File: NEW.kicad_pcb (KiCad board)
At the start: 2 copper layers, 106 x 80 mm, 16 parts, among them J1 Screw_Terminal_01x16, J2 Screw_Terminal_01x16, J3 buck converter, J4 Infrared, J5 BMI, J6 light sensor, Q1 PN2222A, U1 LM1117T-5.0, U2 ESP32-CAM

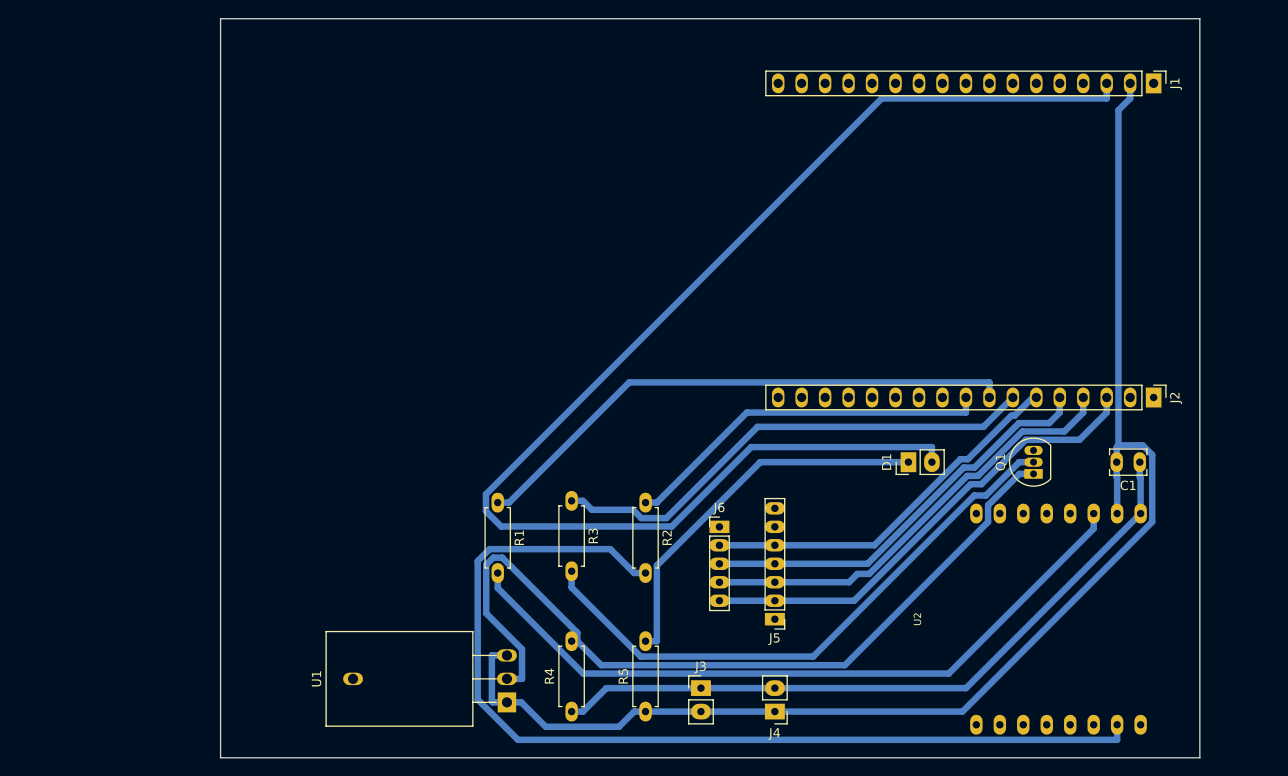
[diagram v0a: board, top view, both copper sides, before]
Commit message: added mounting holes
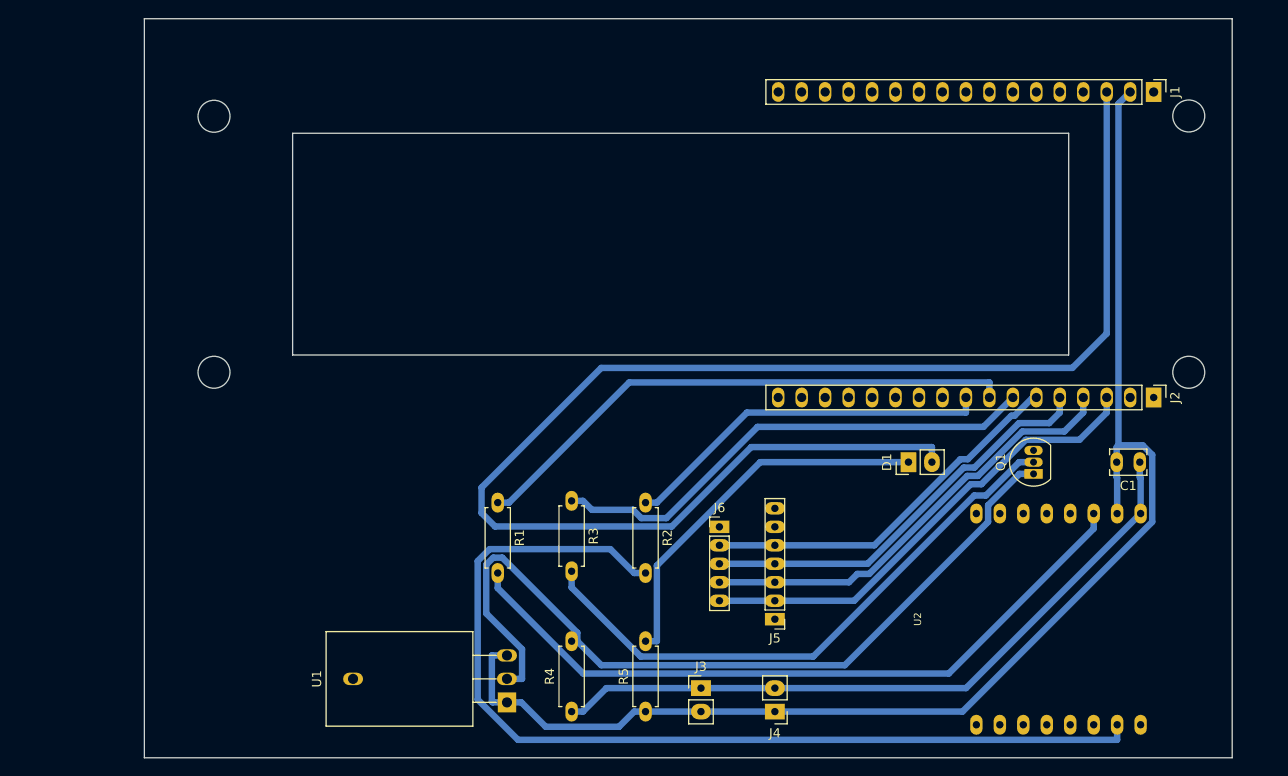
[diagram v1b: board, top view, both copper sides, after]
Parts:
- moved J1 0.93 mm to (219.0, 53.9)
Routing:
- net Net-(D1-A): track 142.6 -> 158.0 mm
- net GND: track 147.0 -> 146.0 mm
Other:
- board size 106 x 80 mm -> 117.8 x 80 mm
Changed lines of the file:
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@@
 	(footprint "Connector_PinHeader_2.54mm:PinHeader_1x17_P2.54mm_Vertical"
 		(layer "F.Cu")
-		(at 219 53 -90)
+		(at 219 53.93 -90)
 		(descr "Through hole straight pin header, 1x17, 2.54mm pitch, single row")
 		(tags "Through hole pin header THT 1x17 2.54mm single row")
@@
 	)
 	(gr_rect
-		(start 118 46)
-		(end 224 126)
+		(start 109.75 46)
+		(end 227.5 126)
+		(stroke
+			(width 0.05)
+			(type default)
+		)
+		(fill none)
+		(layer "Edge.Cuts")
+	)
+	(gr_circle
+		(center 222.8 56.53)
+		(end 221.07 56.53)
+		(stroke
+			(width 0.05)
+			(type default)
+		)
+		(fill none)
+		(layer "Edge.Cuts")
+	)
+	(gr_circle
+		(center 117.29 56.56)
+		(end 115.56 56.56)
+		(stroke
+			(width 0.05)
+			(type default)
+		)
+		(fill none)
+		(layer "Edge.Cuts")
+	)
+	(gr_circle
+		(center 117.29 84.27)
+		(end 115.56 84.27)
+		(stroke
+			(width 0.05)
+			(type default)
+		)
+		(fill none)
+		(layer "Edge.Cuts")
+	)
+	(gr_rect
+		(start 125.8 58.4)
+		(end 209.8 82.4)
+		(stroke
+			(width 0.05)
+			(type default)
+		)
+		(fill none)
+		(layer "Edge.Cuts")
+	)
+	(gr_circle
+		(center 222.8 84.27)
+		(end 221.07 84.27)
 		(stroke
 			(width 0.05)
@@
 	)
 	(segment
-		(start 215.19 55.9017)
-		(end 215.19 92.1783)
-		(width 0.7)
-		(layer "B.Cu")
-		(net 1)
-	)
-	(segment
 		(start 153.1946 122.6429)
 		(end 150.5517 120)
@@
 	)
 	(segment
-		(start 216.46 54.6317)
-		(end 215.19 55.9017)
-		(width 0.7)
-		(layer "B.Cu")
-		(net 1)
-	)
-	(segment
 		(start 149 114.92)
 		(end 147.3683 114.92)
@@
 	)
 	(segment
-		(start 216.46 53)
-		(end 216.46 54.6317)
-		(width 0.7)
-		(layer "B.Cu")
-		(net 1)
-	)
-	(segment
 		(start 217.8183 92.1783)
 		(end 215.19 92.1783)
@@
 	)
 	(segment
+		(start 215.19 92.1783)
+		(end 215.19 55.2)
+		(width 0.7)
+		(layer "B.Cu")
+		(net 1)
+	)
+	(segment
+		(start 215.19 55.2)
+		(end 216.46 53.93)
+		(width 0.7)
+		(layer "B.Cu")
+		(net 1)
+	)
+	(segment
 		(start 149 120)
 		(end 150.5517 120)
@@
 	)
 	(segment
-		(start 146.7271 97.4727)
-		(end 146.7271 99.3193)
+		(start 166.8427 100.9615)
+		(end 147.7115 100.9615)
 		(width 0.7)
 		(layer "B.Cu")
@@
 	)
 	(segment
-		(start 146.7271 99.3193)
-		(end 148.3693 100.9615)
+		(start 159.2 83.8)
+		(end 210.2 83.8)
 		(width 0.7)
 		(layer "B.Cu")
@@
 	)
 	(segment
-		(start 213.92 53)
-		(end 213.92 54.6317)
+		(start 175.4359 92.3683)
+		(end 166.8427 100.9615)
 		(width 0.7)
 		(layer "B.Cu")
@@
 	)
 	(segment
-		(start 148.3693 100.9615)
-		(end 166.8427 100.9615)
+		(start 210.2 83.8)
+		(end 213.92 80.08)
 		(width 0.7)
 		(layer "B.Cu")
@@
 	)
 	(segment
-		(start 166.8427 100.9615)
-		(end 175.4359 92.3683)
+		(start 146.25 96.75)
+		(end 159.2 83.8)
+		(width 0.7)
+		(layer "B.Cu")
+		(net 3)
+	)
+	(segment
+		(start 147.7115 100.9615)
+		(end 146.25 99.5)
 		(width 0.7)
 		(layer "B.Cu")
@@
 	)
 	(segment
-		(start 189.5681 54.6317)
-		(end 146.7271 97.4727)
+		(start 213.92 80.08)
+		(end 213.92 53.93)
 		(width 0.7)
 		(layer "B.Cu")
@@
 	)
 	(segment
-		(start 213.92 54.6317)
-		(end 189.5681 54.6317)
+		(start 195 92.3683)
+		(end 175.4359 92.3683)
 		(width 0.7)
 		(layer "B.Cu")
@@
 	)
 	(segment
-		(start 175.4359 92.3683)
-		(end 195 92.3683)
+		(start 146.25 99.5)
+		(end 146.25 96.75)
 		(width 0.7)
 		(layer "B.Cu")
@@
 		(net 43)
 	)
+	(group ""
+		(members "2858ad9e-ec96-459c-ba4e-2edf304c7cb4" "dd17c023-4089-4896-95e1-fccc1c4ef407")
+	)
+	(group ""
+		(members "0f42caad-e9f0-48f2-8db3-a60ad6f021ee" "c0290355-8473-48cf-b4b2-91f21fcba8cf")
+	)
+	(group ""
+		(members "87d010a2-113f-4a3d-9e5c-7e4fa9d92f45" "ab4ddfdb-e27a-49dc-848d-2c798d915fe7")
+	)
+	(group ""
+		(members "3f69567e-cf5b-4299-bfce-c0d687d98717" "e9279e01-e234-4650-8447-3c4098cbc3b9")
+	)
 )

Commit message: added silkscreen for boost converter
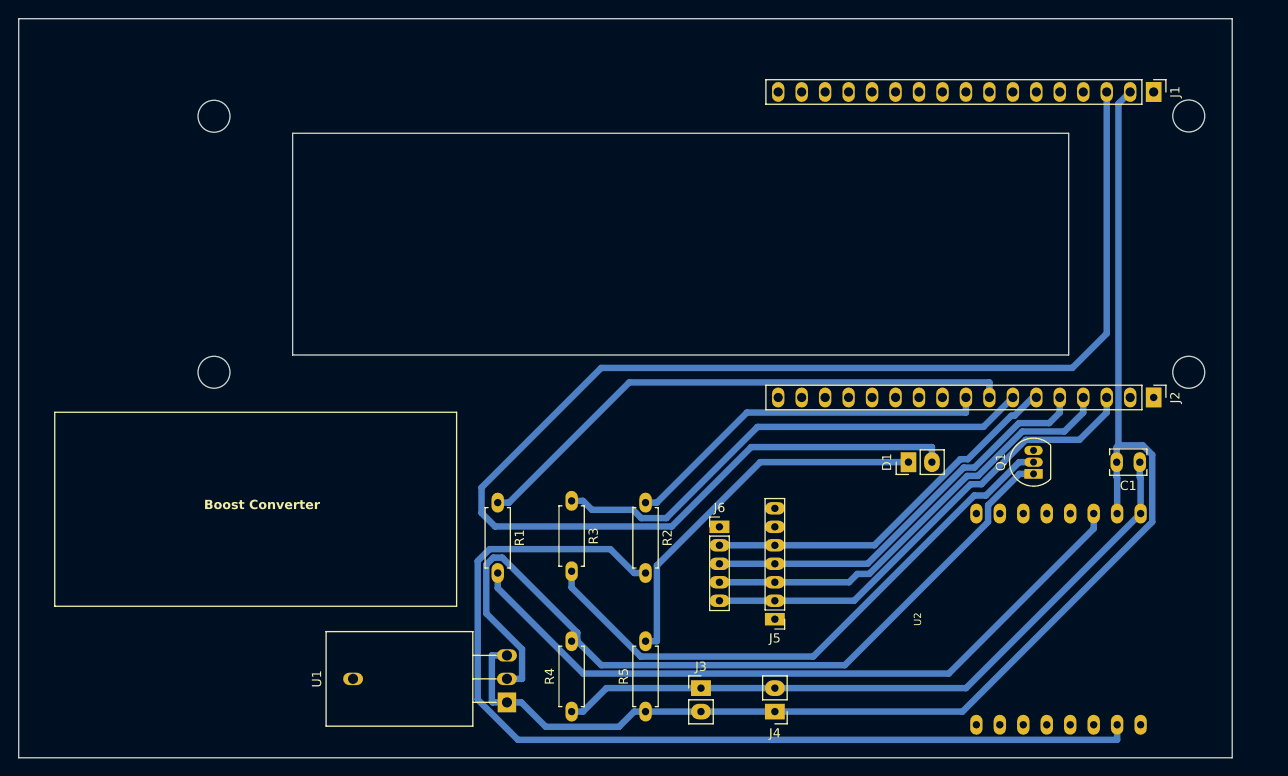
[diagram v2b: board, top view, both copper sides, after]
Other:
- board size 117.8 x 80 mm -> 131.3 x 80 mm
- board text added: "Boost Converter"
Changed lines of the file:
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@@
 	)
 	(gr_rect
-		(start 109.75 46)
+		(start 100.05 88.6)
+		(end 143.55 109.6)
+		(stroke
+			(width 0.1)
+			(type default)
+		)
+		(fill none)
+		(layer "F.SilkS")
+	)
+	(gr_rect
+		(start 96.15 46)
 		(end 227.5 126)
 		(stroke
@@
 		(layer "Edge.Cuts")
 	)
+	(gr_text "Boost Converter"
+		(at 116.2 99.2 0)
+		(layer "F.SilkS")
+		(effects
+			(font
+				(size 1 1)
+				(thickness 0.2)
+				(bold yes)
+			)
+			(justify left bottom)
+		)
+	)
 	(segment

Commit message: chore: update project files
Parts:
- added C2: C_Polarized_Small, Capacitor_THT:C_Disc_D3.8mm_W2.6mm_P2.50mm, F.Cu at (114.5, 117.5)
- added J7: servo, Connector_PinHeader_2.54mm:PinHeader_1x03_P2.54mm_Vertical, F.Cu at (109.6, 115.2)
- J4: footprint Connector_PinHeader_2.54mm:PinHeader_1x02_P2.54mm_Vertical -> Connector_PinHeader_2.54mm:PinHeader_1x03_P2.54mm_Vertical
- moved J5 7.28 mm to (180.0, 104.0), turned to -90 degrees
- moved J6 7.28 mm to (170.0, 94.0), turned to 90 degrees
- moved R2 6.52 mm to (159.0, 94.2)
- moved R3 4.85 mm to (153.0, 94.4)
- moved R1 4.00 mm to (148.0, 94.4)
- moved J3 2.54 mm to (170.0, 121.0), turned to 180 degrees
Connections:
- J1 pad 13: unconnected-(J1-Pin_13-Pad13) -> Net-(J1-Pin_13)
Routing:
- net Net-(J2-Pin_5): track 45.3 -> 209.5 mm
- net GND: track 146.0 -> 0.00 mm
- net Net-(J1-Pin_13): track 0.00 -> 131.1 mm
- net VCC: track 76.1 -> 206.0 mm
- net Net-(R1-Pad2): track 78.1 -> 189.0 mm
- net Net-(J2-Pin_6): track 40.9 -> 104.0 mm
- net Net-(D1-A): track 158.0 -> 102.2 mm
- net Net-(Q1-E): track 90.8 -> 71.2 mm
- net Net-(R2-Pad2): track 107.4 -> 100.8 mm
- net Net-(J2-Pin_9): track 40.3 -> 45.2 mm
- net Net-(D1-K): track 41.3 -> 38.0 mm
- net Net-(J2-Pin_7): track 53.9 -> 56.1 mm
- net Net-(J2-Pin_3): track 52.0 -> 50.0 mm
- net Net-(J2-Pin_4): track 48.6 -> 50.5 mm
- net Net-(Q1-B): track 63.6 -> 64.8 mm
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- added copper zone on B.Cu, net GND

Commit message: Update KiCad project files
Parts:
- added C3: C_Polarized_Small, Capacitor_THT:C_Disc_D3.8mm_W2.6mm_P2.50mm, F.Cu at (123.0, 119.0)
- added J8: Screw_Terminal_01x03, Connector_PinHeader_2.54mm:PinHeader_1x03_P2.54mm_Vertical, F.Cu at (198.5, 50.0)
- added J9: battery +, Connector_PinHeader_2.54mm:PinHeader_1x01_P2.54mm_Vertical, F.Cu at (101.0, 121.0)
- J1, J2: footprint Connector_PinHeader_2.54mm:PinHeader_1x17_P2.54mm_Vertical -> Connector_PinHeader_2.54mm:PinHeader_1x16_P2.54mm_Vertical
- J5: footprint Connector_PinHeader_2.00mm:PinHeader_1x07_P2.00mm_Vertical -> Connector_PinHeader_2.54mm:PinHeader_1x07_P2.54mm_Vertical
- J6: footprint Connector_PinHeader_2.00mm:PinHeader_1x05_P2.00mm_Vertical -> Connector_PinHeader_2.54mm:PinHeader_1x05_P2.54mm_Vertical
- moved R2 65.3 mm to (223.0, 107.2)
- moved R1 54.9 mm to (201.2, 108.0), turned to 0 degrees
- moved Q1 52.1 mm to (155.0, 106.0), turned to 180 degrees
- moved R3 44.1 mm to (195.8, 105.0), turned to 180 degrees
- moved D1 26.1 mm to (170.5, 108.0)
- moved J5 18.2 mm to (162.0, 101.2), turned to 180 degrees
- moved C1 14.0 mm to (217.5, 108.0)
- moved J6 4.12 mm to (171.0, 90.0), turned to 0 degrees
- moved C2 2.50 mm to (116.0, 119.5), turned to -90 degrees
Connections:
- J1 pad 13: Net-(J1-Pin_13) -> unconnected-(J1-Pin_13-Pad13)
- J1 pad 14: unconnected-(J1-Pin_14-Pad14) -> Net-(J1-Pin_14)
- J1 pad 16: unconnected-(J1-Pin_16-Pad16) -> Net-(J1-Pin_16)
- J1 pad 8: unconnected-(J1-Pin_8-Pad8) -> Net-(J1-Pin_8)
- J1 pad 9: unconnected-(J1-Pin_9-Pad9) -> Net-(J1-Pin_9)
- J4 pad 2: VCC -> Net-(J1-Pin_16)
- J7 pad 1: Net-(J1-Pin_13) -> Net-(J1-Pin_14)
- Q1 pad 3: unconnected-(Q1-C-Pad3) -> GND
- U2 pad IO12: Net-(R1-Pad2) -> unconnected-(U2-PadIO12)
- U2 pad IO13: unconnected-(U2-PadIO13) -> Net-(R1-Pad2)
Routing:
- net Net-(J1-Pin_16): track 0.00 -> 277.9 mm
- net Net-(J2-Pin_9): track 45.2 -> 288.1 mm
- net GND: track 0.00 -> 232.4 mm
- net Net-(J1-Pin_14): track 0.00 -> 182.0 mm
- net Net-(R1-Pad2): track 189.0 -> 8.92 mm
- net Net-(J2-Pin_5): track 209.5 -> 50.8 mm
- net Net-(J1-Pin_13): track 131.1 -> 0.00 mm
- net Net-(R2-Pad2): track 100.8 -> 15.6 mm
- net VCC: track 206.0 -> 145.7 mm
- net Net-(J2-Pin_6): track 104.0 -> 48.4 mm
- net Net-(Q1-E): track 71.2 -> 16.8 mm
- net Net-(Q1-B): track 64.8 -> 36.4 mm
- net Net-(D1-K): track 38.0 -> 11.8 mm
- net Net-(D1-A): track 102.2 -> 113.6 mm
- net Net-(J2-Pin_7): track 56.1 -> 45.9 mm
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- removed copper zone on B.Cu, net GND
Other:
- board size 131.3 x 80 mm -> 135.3 x 80 mm
